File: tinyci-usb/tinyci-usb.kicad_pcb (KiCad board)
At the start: 2 copper layers, 110 x 82.5 mm, 52 parts, among them J1 Jack-DC, J2 USB_A, J3 USB_A, J4 USB_A, J5 USB_A, J9 Conn_01x04_Male, K1 SANYOU_SRD_Form_C, K2 SANYOU_SRD_Form_C, K3 SANYOU_SRD_Form_C, K4 SANYOU_SRD_Form_C, Q1 BC337, Q2 BC337, Q3 BC337, Q4 BC337, U1 AMS1117-3.3

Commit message: TinyCI USB v0.1
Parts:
- added G***: LOGO, TinyCI:just-ci-it, B.Cu at (165.0, 87.5)

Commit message: Add LICENCE to TinyCI-USB
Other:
- board text added: "TinyCI USB v0.1 http://github.com/superna9999/tinyci CERN OPEN HARDWARE LICENCE v1.1"
- board text removed: "TinyCI USB v0.1 http://github.com/superna9999/tinyci"
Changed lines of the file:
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@@
     (arrow2b (pts (xy 197.5 35) (xy 196.373496 35.586421)))
   )
-  (gr_text "TinyCI USB v0.1\nhttp://github.com/superna9999/tinyci" (at 104.5 87.75 90) (layer B.SilkS)
+  (gr_text "TinyCI USB v0.1\nhttp://github.com/superna9999/tinyci\n\nCERN OPEN HARDWARE LICENCE v1.1" (at 100.5 87.25 90) (layer B.SilkS)
     (effects (font (size 3 2.5) (thickness 0.5)) (justify mirror))
   )

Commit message: Ordered Version !
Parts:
- added USB0: BarrelJack_Horizontal, Connector_BarrelJack:BarrelJack_Horizontal, F.Cu at (189.2, 64.5)
- added USB1: BarrelJack_Horizontal, Connector_BarrelJack:BarrelJack_Horizontal, F.Cu at (189.2, 84.0)
- added USB2: BarrelJack_Horizontal, Connector_BarrelJack:BarrelJack_Horizontal, F.Cu at (189.2, 103.2)
- added USB3: BarrelJack_Horizontal, Connector_BarrelJack:BarrelJack_Horizontal, F.Cu at (189.5, 122.0)
- J2, J3, J4, J5: footprint Connector_USB:USB_A_Molex_105057_Vertical -> Connector_USB:USB_A_Stewart_SS-52100-001_Horizontal
- moved J2 9.15 mm to (186.0, 66.2), turned to 90 degrees
- moved J3 8.95 mm to (186.0, 86.0), turned to 90 degrees
- moved J4 8.95 mm to (186.0, 105.0), turned to 90 degrees
- moved J5 8.36 mm to (186.0, 123.8), turned to 90 degrees
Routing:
- net Net-(C2-Pad1): track 40.0 -> 30.9 mm
- net Net-(C4-Pad1): track 35.4 -> 28.8 mm
- net Net-(C6-Pad1): track 30.5 -> 33.6 mm
- net Net-(C5-Pad1): track 31.3 -> 28.9 mm
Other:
- board text added: "DC 5V DC 5V-12V"
- board text added: "JLCJLCJLCJLC"
- board text removed: "DC 5V"
- board text removed: "IO12"
- board text removed: "IO17"
- board text removed: "IO32"
- board text removed: "IO33"
- board text removed: "IO5"

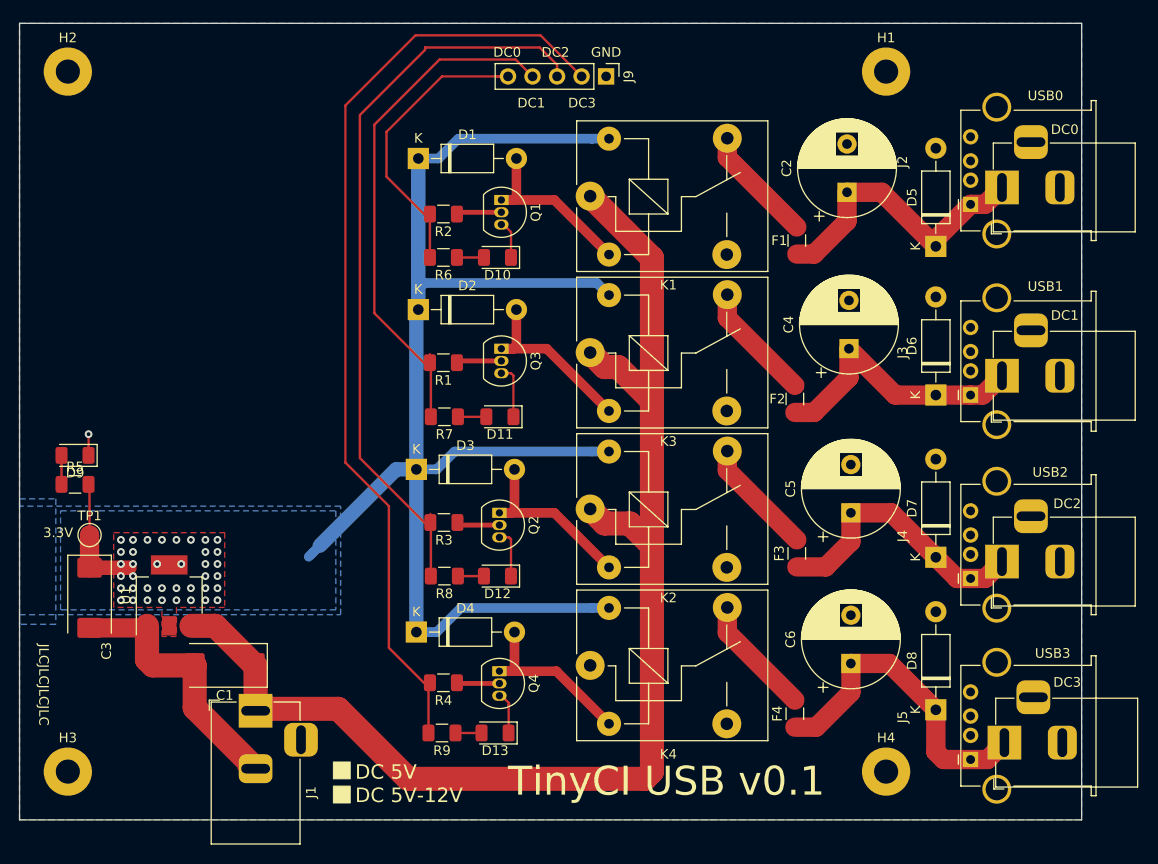
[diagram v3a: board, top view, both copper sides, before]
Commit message: TinyCI USB 0.2
- Updated schematic with correct USB Type A footprint
- Fixed bad relay output (outputs must be disabled by default, activating the relay will send power to outputs)
- removed LDO
- added DC-DC screw terminal footprint + drawing of LM2596 DC-DC module to solder
- grow mounting hole to 3.2mm to target M3 screws
- relay 4 was missing Vinput signal to pin 1
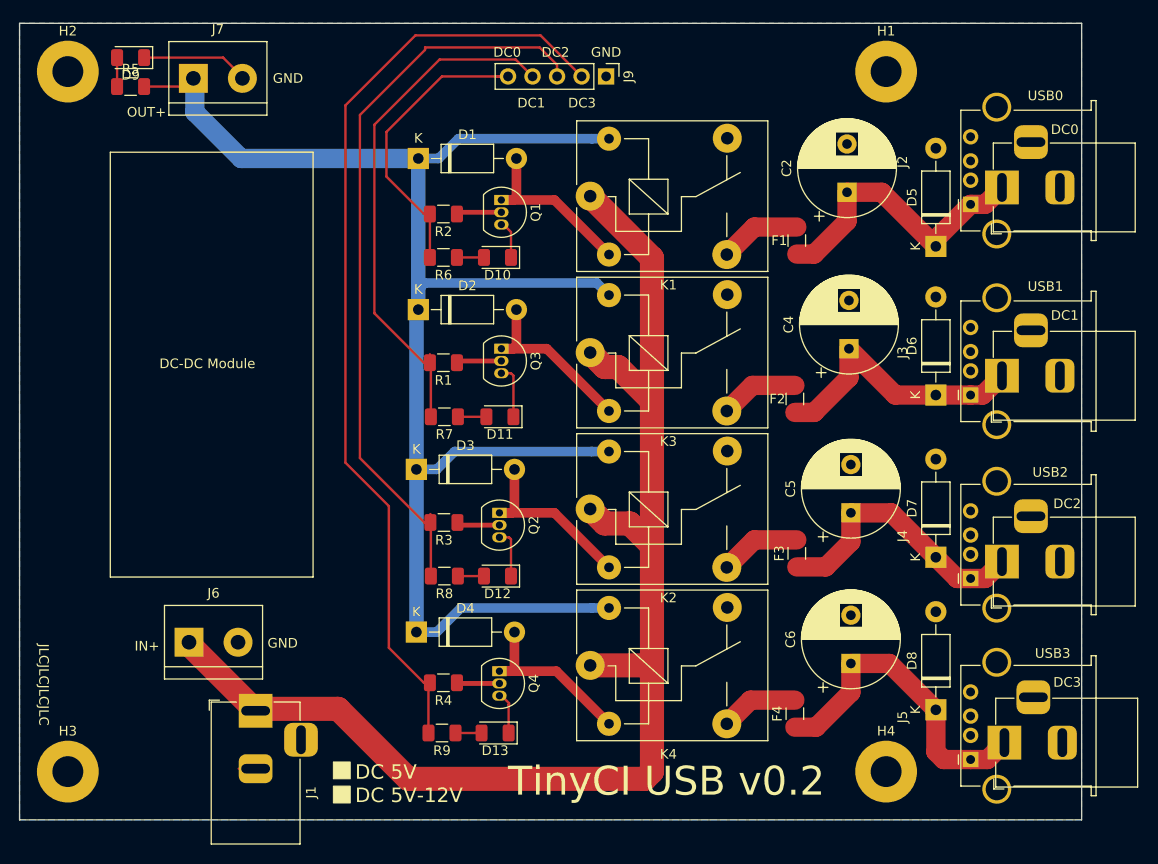
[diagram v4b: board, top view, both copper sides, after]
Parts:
- removed C1, C3: 10uF, Capacitor_Tantalum_SMD:CP_EIA-7343-31_Kemet-D
- removed TP1: TestPoint, TestPoint:TestPoint_Pad_D2.0mm
- removed U1: AMS1117-3.3, Package_TO_SOT_SMD:SOT-223-3_TabPin2
- added J6: Screw_Terminal_01x02, TerminalBlock:TerminalBlock_bornier-2_P5.08mm, F.Cu at (105.0, 111.6)
- added J7: Screw_Terminal_01x02, TerminalBlock:TerminalBlock_bornier-2_P5.08mm, F.Cu at (105.5, 53.2)
- H1, H2, H3, H4: footprint MountingHole:MountingHole_2.5mm_Pad -> MountingHole:MountingHole_3.2mm_M3_Pad
- moved D9 41.6 mm to (99.0, 51.0)
- moved R5 41.6 mm to (99.0, 54.0)
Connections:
- net +5V renamed +VDC
- K1 pad 3: Net-(K1-Pad3) -> /NO_1
- K1 pad 4: /NO_1 -> Net-(K1-Pad4)
- K2 pad 3: Net-(K2-Pad3) -> /NO_3
- K2 pad 4: /NO_3 -> Net-(K2-Pad4)
- K3 pad 3: Net-(K3-Pad3) -> /NO_2
- K3 pad 4: /NO_2 -> Net-(K3-Pad4)
- K4 pad 3: Net-(K4-Pad3) -> /NO_4
- K4 pad 4: /NO_4 -> Net-(K4-Pad4)
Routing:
- net GND: track 51.7 -> 32.7 mm, vias 1 -> 0
- net +3V3: track 163.0 -> 168.6 mm, vias 38 -> 0
- net /NO_4: track 12.5 -> 8.06 mm
- net /NO_2: track 12.3 -> 8.15 mm
- net /NO_3: track 12.2 -> 8.43 mm
- net /NO_1: track 12.2 -> 8.43 mm
- net +VDC: track 136.6 -> 139.9 mm
- removed copper zone on B.Cu, net +3V3
- removed copper zone on F.Cu, net +3V3
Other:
- board text added: "DC-DC Module"
- board text added: "IN+"
- board text added: "OUT+"
- board text added: "TinyCI USB v0.2"
- board text removed: "3.3V"
- board text removed: "TinyCI USB v0.1"

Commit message: TinyCI USB 0.3
Remove post-relay protections, and move 1000uF caps before relay.

Add proper OSHW & Made with KiCad logo

Signed-off-by: Neil Armstrong <narmstrong@baylibre.com>
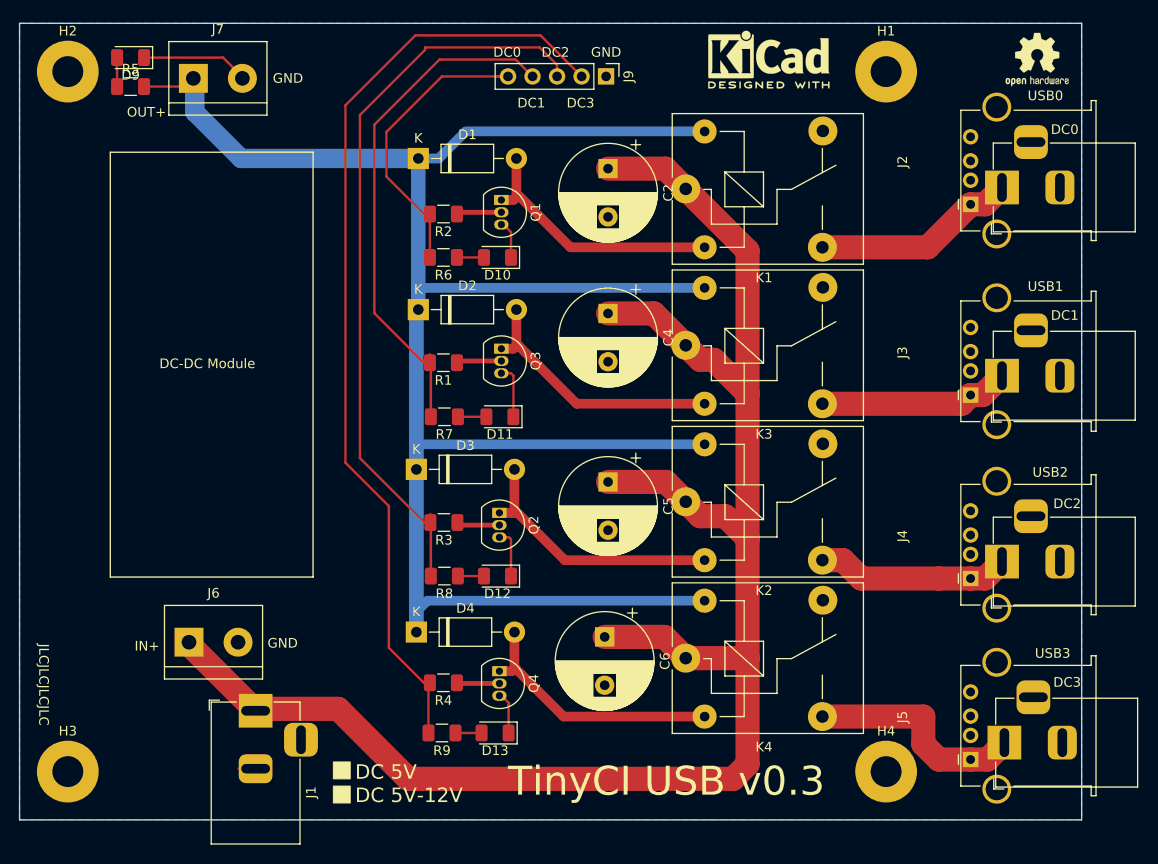
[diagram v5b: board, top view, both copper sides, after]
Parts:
- removed D5, D6, D7, D8: 1N4001, Diode_THT:D_DO-41_SOD81_P10.16mm_Horizontal
- removed F1, F2, F3, F4: Polyfuse, Fuse:Fuse_1206_3216Metric
- added REF**: OSHW-Logo2_7.3x6mm_SilkScreen, Symbol:OSHW-Logo2_7.3x6mm_SilkScreen, F.Cu at (192.9, 51.2)
- added REF**: KiCad-Logo2_5mm_SilkScreen, Symbol:KiCad-Logo2_5mm_SilkScreen, F.Cu at (165.1, 51.2)
- moved C6 25.6 mm to (148.1, 111.0), turned to 270 degrees
- moved C5 25.4 mm to (148.4, 95.0), turned to 270 degrees
- moved C4 25.2 mm to (148.4, 77.5), turned to 270 degrees
- moved C2 24.9 mm to (148.4, 62.5), turned to 270 degrees
- moved K1 9.93 mm to (156.5, 64.7)
- moved K2 9.93 mm to (156.5, 97.0)
- moved K3 9.93 mm to (156.5, 80.8)
- moved K4 9.93 mm to (156.5, 113.2)
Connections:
- C2 pad 1: Net-(C2-Pad1) -> +VDC
- C4 pad 1: Net-(C4-Pad1) -> +VDC
- C5 pad 1: Net-(C5-Pad1) -> +VDC
- C6 pad 1: Net-(C6-Pad1) -> +VDC
- J2 pad 1: Net-(C2-Pad1) -> /NO_1
- J3 pad 1: Net-(C4-Pad1) -> /NO_2
- J4 pad 1: Net-(C5-Pad1) -> /NO_3
- J5 pad 1: Net-(C6-Pad1) -> /NO_4
- USB0 pad 1: Net-(C2-Pad1) -> /NO_1
- USB1 pad 1: Net-(C4-Pad1) -> /NO_2
- USB2 pad 1: Net-(C5-Pad1) -> /NO_3
- USB3 pad 1: Net-(C6-Pad1) -> /NO_4
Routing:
- net +VDC: track 139.9 -> 186.7 mm
- net +3V3: track 168.6 -> 210.9 mm
- net Net-(C6-Pad1): track 33.6 -> 0.00 mm
- net Net-(C2-Pad1): track 30.9 -> 0.00 mm
- net Net-(C5-Pad1): track 28.9 -> 0.00 mm
- net Net-(C4-Pad1): track 28.8 -> 0.00 mm
- net /NO_4: track 8.06 -> 23.1 mm
- net /NO_1: track 8.43 -> 21.2 mm
- net /NO_3: track 8.43 -> 20.1 mm
- net /NO_2: track 8.15 -> 19.8 mm
- net /COIL_1_3: track 19.6 -> 28.2 mm
- net /COIL_1_2: track 19.3 -> 27.4 mm
- net /COIL_1_4: track 19.0 -> 27.2 mm
- net /COIL_1_1: track 19.2 -> 27.3 mm
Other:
- board text added: "TinyCI USB v0.3"
- board text added: "TinyCI USB v0.3 http://github.com/superna9999/tinyci CERN OPEN HARDWARE LICENCE v1.1"
- board text removed: "TinyCI USB v0.1 http://github.com/superna9999/tinyci CERN OPEN HARDWARE LICENCE v1.1"
- board text removed: "TinyCI USB v0.2"
